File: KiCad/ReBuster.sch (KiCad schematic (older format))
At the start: 13 parts, among them U3 SN74CBTD16210, U4 SN74LVC16T245DGVR, U5 SN74CBTD16210, U6 SN74CBTD16210, U7 74LVC2T45DC, U8 PLCC_84_plug, U9 PLCC_84_plug

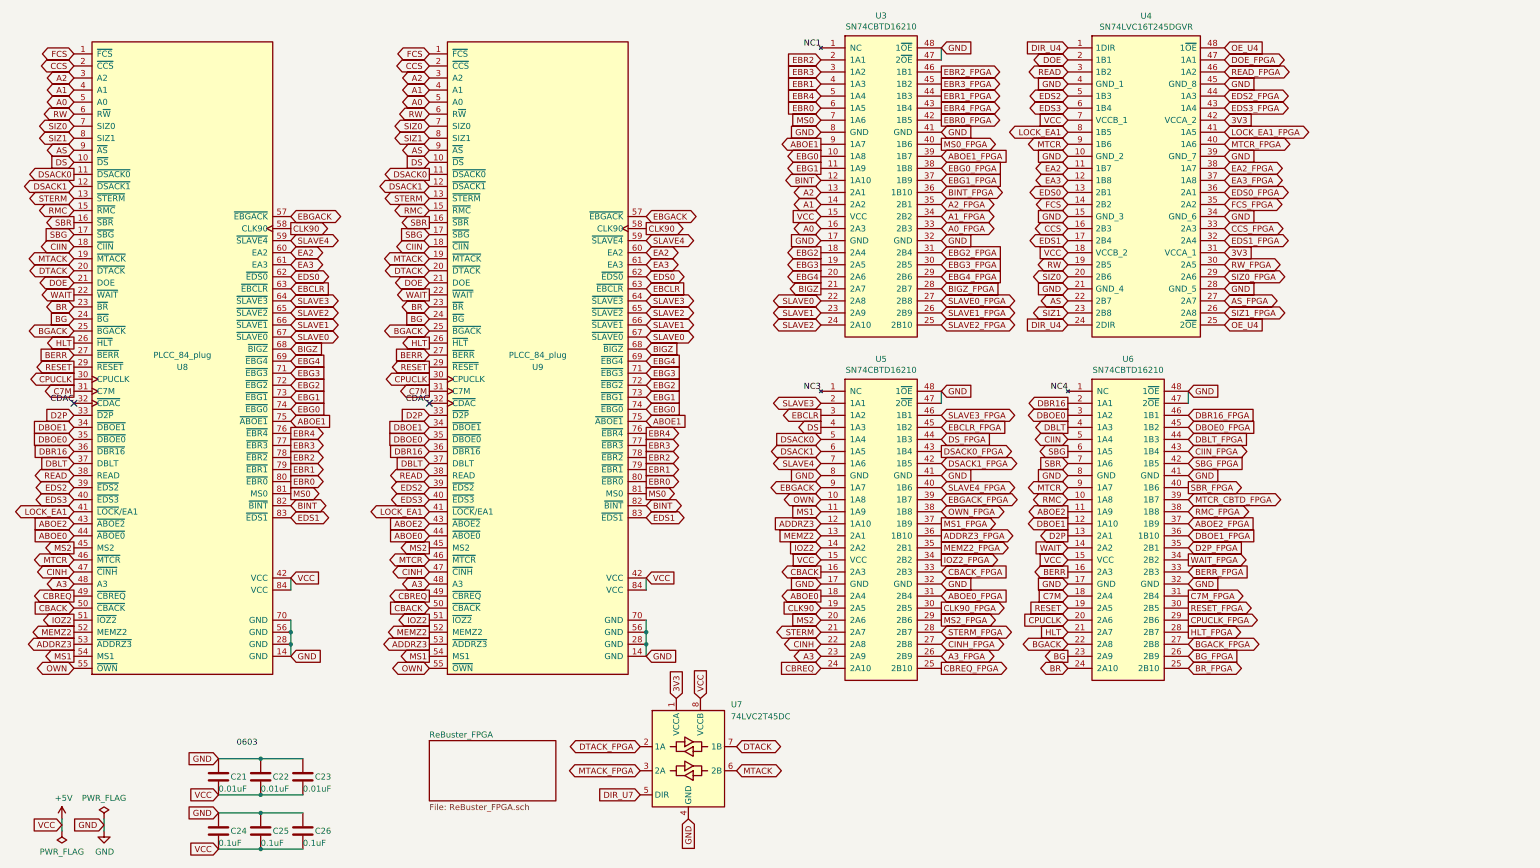
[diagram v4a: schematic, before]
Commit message: remove HLT-signal (not used) and put /DTACK signal there
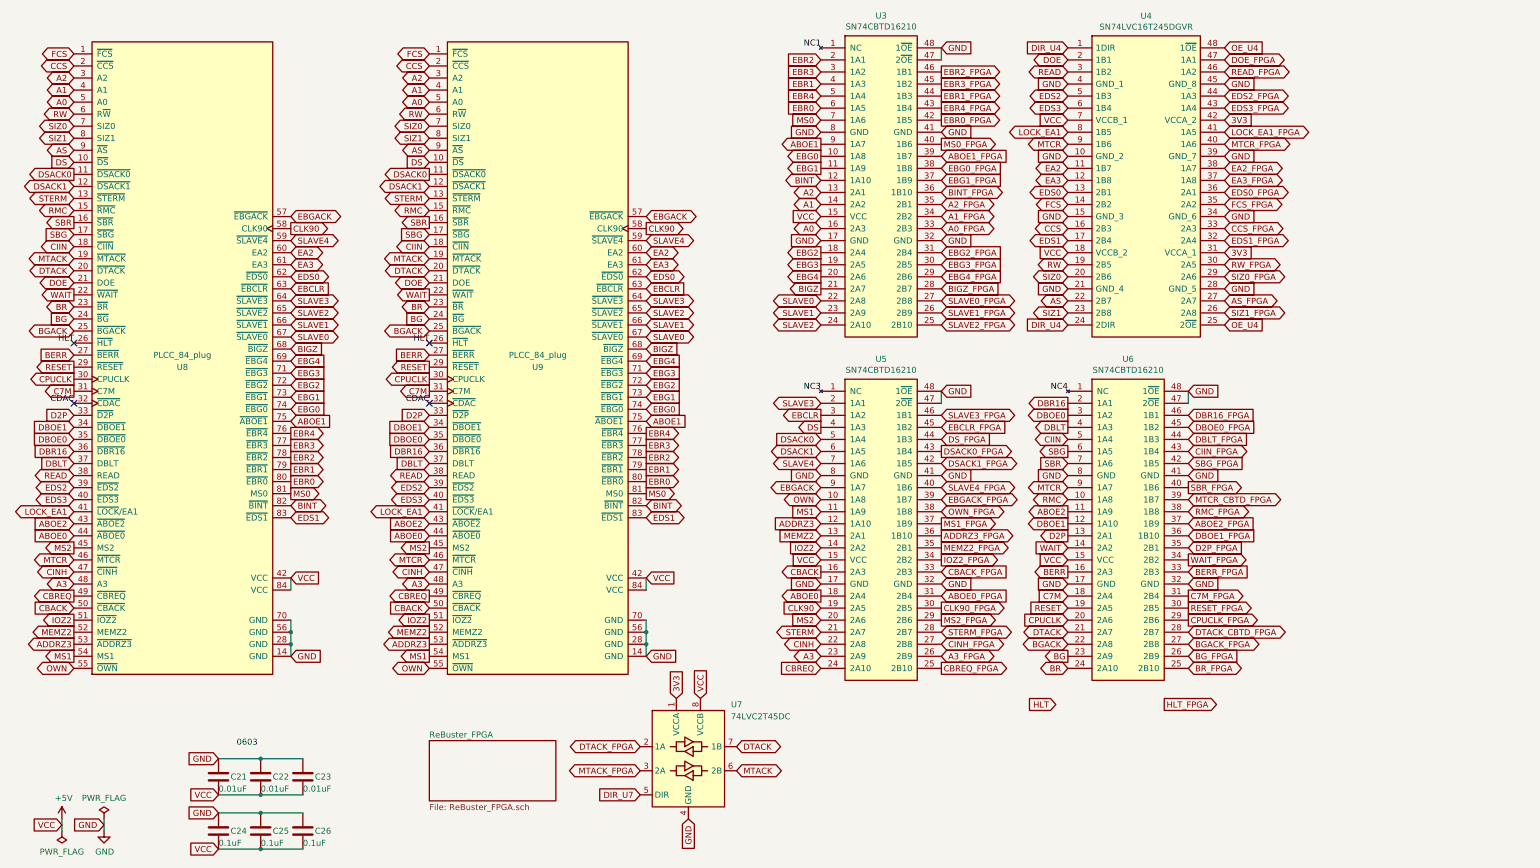
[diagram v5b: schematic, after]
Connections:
- net DTACK: now also U6.21 (2A7)
- net HLT: no longer U6.21 (2A7)
- net HLT_FPGA: no longer U6.28 (2B7)
- new net DTACK_CBTD_FPGA: U6.28 (2B7)
- no-connect marks 2 -> 4
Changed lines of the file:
@@
 Text GLabel 10200 5500 2    50   Output ~ 0
 C7M_FPGA
-Text GLabel 10200 5800 2    50   Output ~ 0
+Text GLabel 10000 6400 2    50   Output ~ 0
 HLT_FPGA
 Text GLabel 10200 5700 2    50   Output ~ 0
@@
 Text GLabel 950  4400 0    50   Input ~ 0
 DBLT
-Text GLabel 950  3400 0    50   Output ~ 0
-HLT
 Text GLabel 950  3600 0    50   Output ~ 0
 RESET
@@
 Text GLabel 9200 5900 0    50   BiDi ~ 0
 BGACK
-Text GLabel 9200 5800 0    50   Input ~ 0
+Text GLabel 9100 6400 0    50   Input ~ 0
 HLT
 Text GLabel 9200 5300 0    50   Output ~ 0
@@
 Text GLabel 3900 4400 0    50   Input ~ 0
 DBLT
-Text GLabel 3900 3400 0    50   Output ~ 0
-HLT
 Text GLabel 3900 3600 0    50   Output ~ 0
 RESET
@@
 Text GLabel 9200 4600 0    50   BiDi ~ 0
 MTCR
+Text GLabel 9200 5800 0    50   BiDi ~ 0
+DTACK
+Text GLabel 10200 5800 2    50   BiDi ~ 0
+DTACK_CBTD_FPGA
+Text Label 950  3400 2    50   ~ 0
+HLT
+NoConn ~ 950  3400
+Text Label 3900 3400 2    50   ~ 0
+HLT
+NoConn ~ 3900 3400
 $EndSCHEMATC

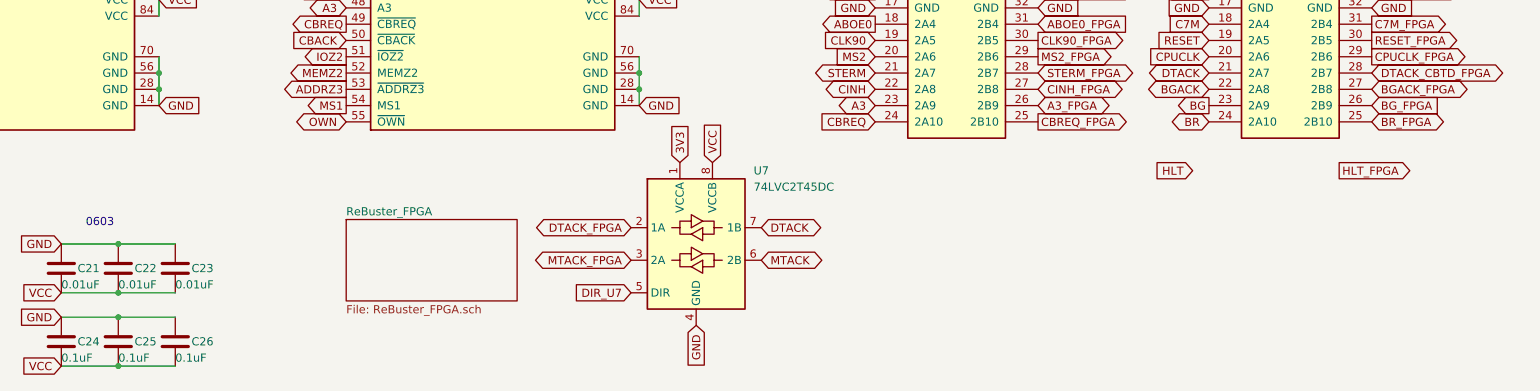
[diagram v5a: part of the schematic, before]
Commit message: Replace 74LVC2T45DC with 74LVC2G07GV and prepare rerouting, reroute /DTACK
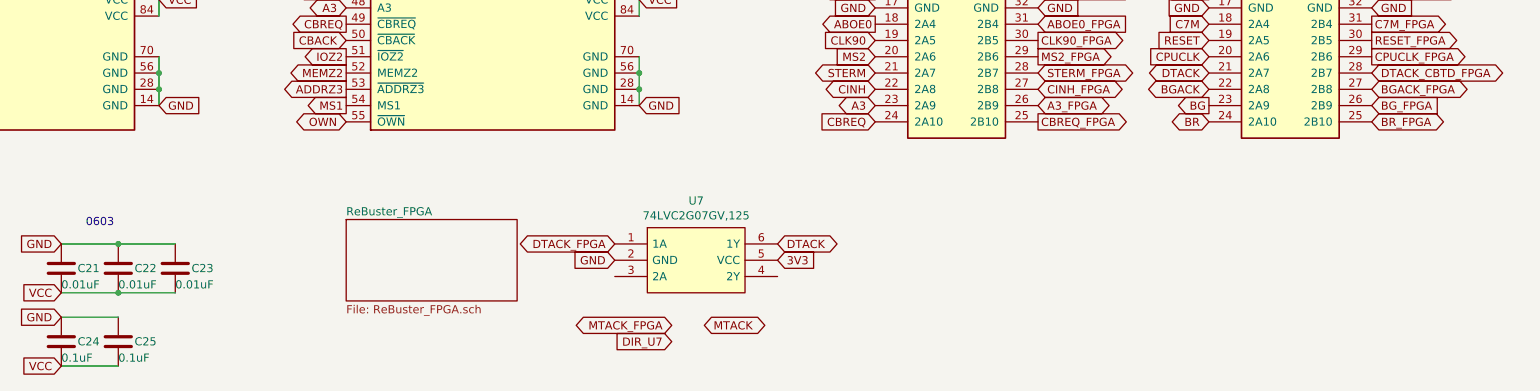
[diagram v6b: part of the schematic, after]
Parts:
- removed C26: 0.1uF, Capacitor_SMD:C_0603_1608Metric_Pad1.08x0.95mm_HandSolder, symbol Device:C
- removed U7: 74LVC2T45DC, Package_SO:VSSOP-8_2.3x2mm_P0.5mm, symbol Logic_LevelTranslator:74LVC2T45DC
- added U7: 74LVC2G07GV,125, Package_SO:TSOP-6_1.65x3.05mm_P0.95mm, symbol ReBuster:74LVC2G07GV,125
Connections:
- net 3V3: now also U7.5 (VCC)
- net DTACK: now also U7.6 (1Y)
- net DTACK_FPGA: now also U7.1 (1A)
- net GND: now also U7.2 (GND)
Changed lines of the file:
@@
 Text GLabel 10500 1050 2    50   BiDi ~ 0
 DOE_FPGA
-Text GLabel 5650 6750 0    50   BiDi ~ 0
+Text GLabel 5550 6850 0    50   BiDi ~ 0
 DTACK_FPGA
-Text GLabel 5650 6950 0    50   BiDi ~ 0
+Text GLabel 5900 7350 0    50   BiDi ~ 0
 MTACK_FPGA
 Text GLabel 10200 4300 2    50   BiDi ~ 0
@@
 Text GLabel 10200 5500 2    50   Output ~ 0
 C7M_FPGA
-Text GLabel 10000 6400 2    50   Output ~ 0
-HLT_FPGA
 Text GLabel 10200 5700 2    50   Output ~ 0
 CPUCLK_FPGA
@@
 Wire Wire Line
 	2750 5350 2750 5450
-Text GLabel 6450 6950 2    50   BiDi ~ 0
+Text GLabel 6100 7350 2    50   BiDi ~ 0
 MTACK
-Text GLabel 6450 6750 2    50   BiDi ~ 0
+Text GLabel 6550 6850 2    50   BiDi ~ 0
 DTACK
 Text GLabel 9200 1050 0    50   BiDi ~ 0
@@
 Text GLabel 9200 5900 0    50   BiDi ~ 0
 BGACK
-Text GLabel 9100 6400 0    50   Input ~ 0
-HLT
 Text GLabel 9200 5300 0    50   Output ~ 0
 BERR
@@
 Text GLabel 10500 2650 2    50   Input ~ 0
 3V3
-$Comp
-L Logic_LevelTranslator:74LVC2T45DC U7
-U 1 1 69AF9BA6
-P 6050 6850
-F 0 "U7" H 6450 7300 50  0000 C CNN
-F 1 "74LVC2T45DC" H 6650 7200 50  0000 C CNN
-F 2 "Package_SO:VSSOP-8_2.3x2mm_P0.5mm" H 6050 6000 50  0001 C CNN
-F 3 "https://assets.nexperia.com/documents/data-sheet/74LVC_LVCH2T45.pdf" H 6300 6600 50  0001 C CNN
-	1    6050 6850
-	1    0    0    -1
-$EndComp
-Text GLabel 5950 6350 1    50   Input ~ 0
+Text GLabel 6550 6950 2    50   Input ~ 0
 3V3
-Text GLabel 6150 6350 1    50   Input ~ 0
-VCC
-Text GLabel 6050 7350 3    50   Input ~ 0
+Text GLabel 5550 6950 0    50   Input ~ 0
 GND
-Text GLabel 5650 7150 0    50   Input ~ 0
+Text GLabel 5900 7450 0    50   Input ~ 0
 DIR_U7
 $Comp
@@
 Wire Wire Line
 	2500 7600 2150 7600
-$Comp
-L Device:C C26
-U 1 1 69EC70AB
-P 2850 7450
-F 0 "C26" H 2950 7450 50  0000 L CNN
-F 1 "0.1uF" H 2850 7350 50  0000 L CNN
-F 2 "Capacitor_SMD:C_0603_1608Metric_Pad1.08x0.95mm_HandSolder" H 2888 7300 50  0001 C CNN
-F 3 "~" H 2850 7450 50  0001 C CNN
-	1    2850 7450
-	1    0    0    -1
-$EndComp
-Wire Wire Line
-	2500 7300 2850 7300
-Connection ~ 2500 7300
-Wire Wire Line
-	2500 7600 2850 7600
-Connection ~ 2500 7600
 Text Label 3900 3900 2    50   ~ 0
 CDAC
@@
 HLT
 NoConn ~ 3900 3400
+$Comp
+L ReBuster:74LVC2G07GV,125 U7
+U 1 1 69FA962F
+P 6050 6950
+F 0 "U7" H 6050 7315 50  0000 C CNN
+F 1 "74LVC2G07GV,125" H 6050 7224 50  0000 C CNN
+F 2 "Package_SO:TSOP-6_1.65x3.05mm_P0.95mm" H 6400 7150 50  0001 L CNN
+F 3 "https://assets.nexperia.com/documents/data-sheet/74LVC2G07.pdf" H 6400 7050 50  0001 L CNN
+	1    6050 6950
+	1    0    0    -1
+$EndComp
 $EndSCHEMATC

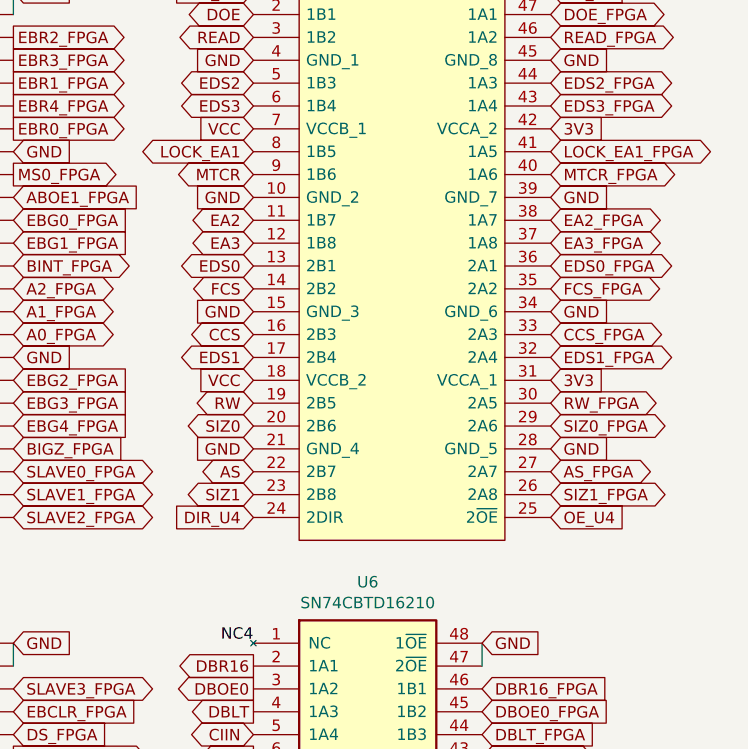
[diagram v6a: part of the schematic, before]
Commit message: Relocate EDS1 signal to replace MTCR's position (pin 9 and 40) in SN74LVC16T245
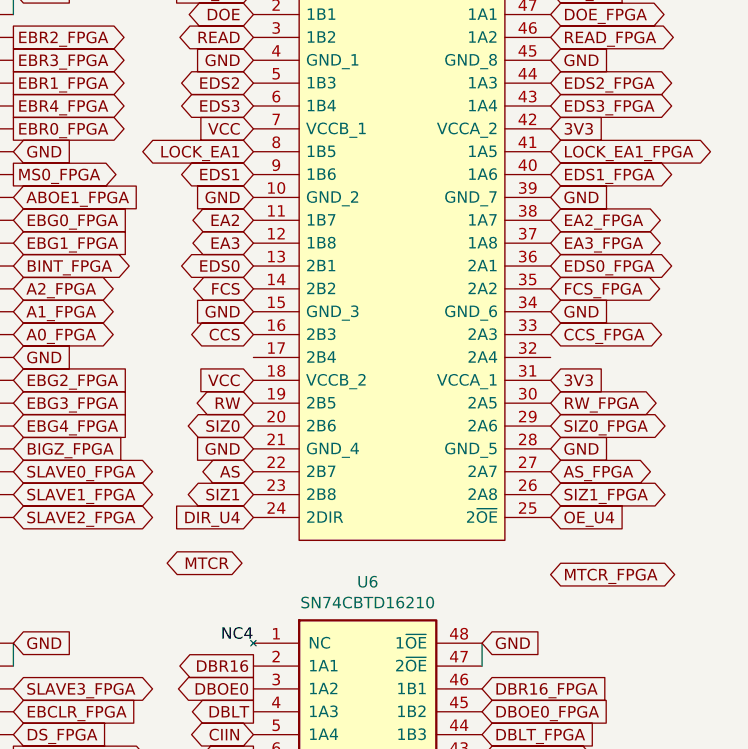
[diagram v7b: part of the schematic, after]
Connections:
- net EDS1: now also U4.9 (1B6); no longer U4.17 (2B4)
- net EDS1_FPGA: now also U4.40 (1A6); no longer U4.32 (2A4)
- net MTCR: no longer U4.9 (1B6)
- net MTCR_FPGA: no longer U4.40 (1A6)
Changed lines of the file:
@@
 Text GLabel 8150 2050 2    50   Input ~ 0
 EBG1_FPGA
-Text GLabel 10500 2550 2    50   BiDi ~ 0
+Text GLabel 10500 1750 2    50   BiDi ~ 0
 EDS1_FPGA
 Text GLabel 10500 2250 2    50   BiDi ~ 0
@@
 Text GLabel 8150 5700 2    50   Output ~ 0
 MS2_FPGA
-Text GLabel 10500 1750 2    50   BiDi ~ 0
+Text GLabel 10500 3500 2    50   BiDi ~ 0
 MTCR_FPGA
 Text GLabel 8150 5900 2    50   BiDi ~ 0
@@
 Text GLabel 7150 5700 0    50   Input ~ 0
 MS2
-Text GLabel 9200 1750 0    50   BiDi ~ 0
+Text GLabel 9150 3450 0    50   BiDi ~ 0
 MTCR
 Text GLabel 2750 4650 2    50   Output ~ 0
@@
 Text GLabel 9200 2050 0    50   BiDi ~ 0
 EA3
-Text GLabel 9200 2550 0    50   BiDi ~ 0
+Text GLabel 9200 1750 0    50   BiDi ~ 0
 EDS1
 Text GLabel 7150 2050 0    50   BiDi ~ 0
